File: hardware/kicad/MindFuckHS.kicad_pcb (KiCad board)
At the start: 2 copper layers, 99.8 x 99.8 mm, 59 parts

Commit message: silk not good
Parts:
- removed the G*** at (0.00, 0.00) (x5)
- added G*** (x2): LOGO, LOGO, F.Cu at (0.00, 0.00)
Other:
- board size 99.8 x 99.8 mm -> 97.1 x 97.3 mm

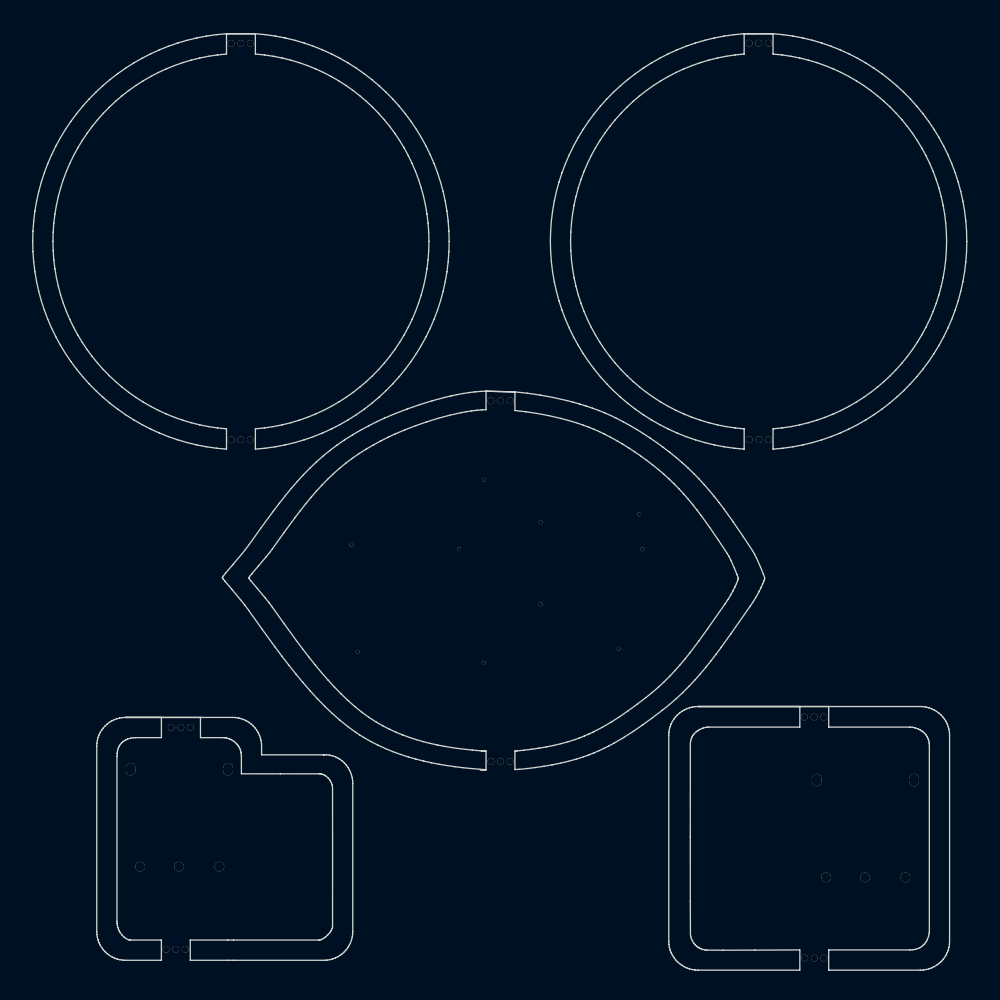
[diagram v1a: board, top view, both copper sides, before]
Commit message: change silk color, add corners
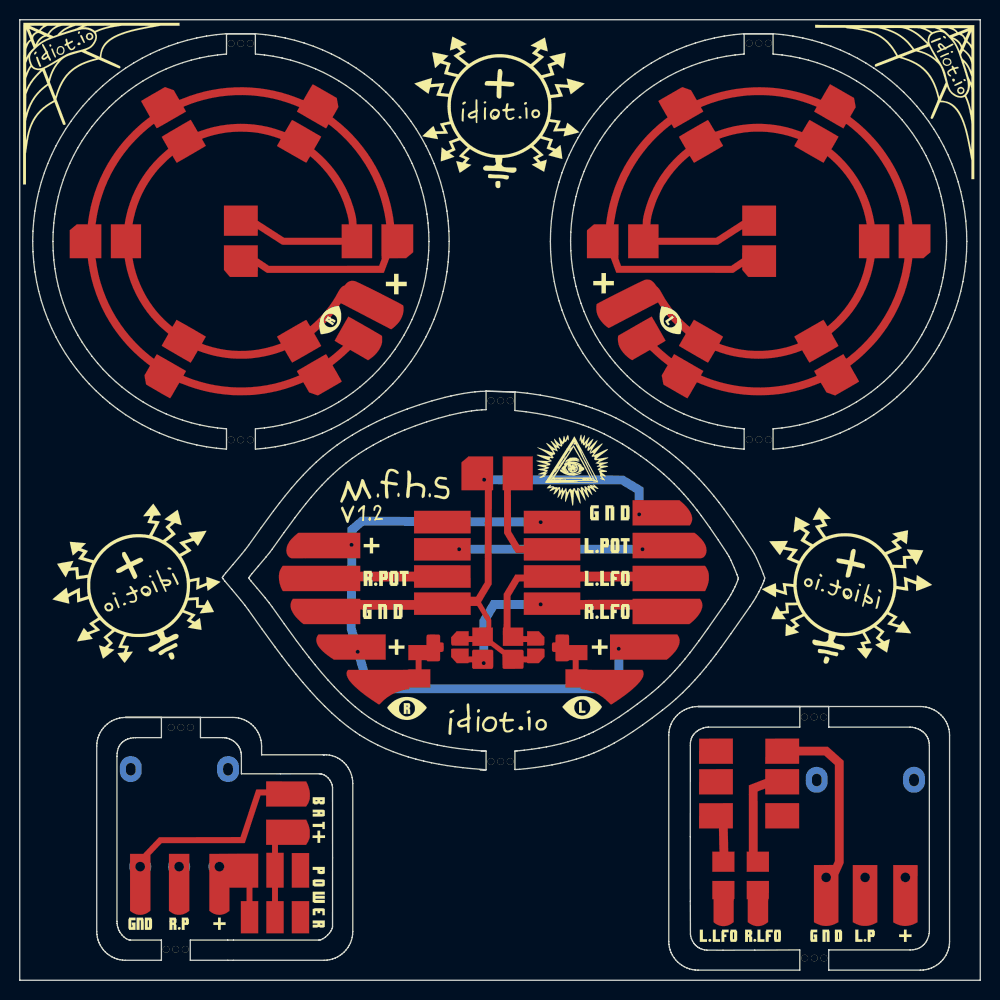
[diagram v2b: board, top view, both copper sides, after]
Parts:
- removed the G*** at (0.00, 0.00) (x2)
- added G*** (x5): LOGO, LOGO, F.Cu at (0.00, 0.00)
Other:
- board size 97.1 x 97.3 mm -> 99.8 x 99.8 mm
